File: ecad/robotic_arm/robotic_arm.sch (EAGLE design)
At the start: 121 parts, among them J1 5A/28V, SW1 5A/28V, Y1 16 MHz

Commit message: Update Robotic Arm to use new EAGLE library names.
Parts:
- A6: device PiB_radio_frequency:ANTENNA_SMD_CHP-2.45GHZ-0.5DBI-3W -> _radio_frequency:ANTENNA_SMD_CHP-2.45GHZ-0.5DBI-3W
- AVR_ISP: device PiB_connectors:AVR_SPI_PRG_6_PTH_VERT_MALE_2.54MM -> _connectors:AVR_SPI_PRG_6_PTH_VERT_MALE_2.54MM
- B1: device PiB_radio_frequency:BALUN_SMD-0805_UNBAL/BAL-50/100 -> _radio_frequency:BALUN_SMD-0805_UNBAL/BAL-50/100
- C1, C10, C12, C14, C16, C19, C2, C22, C24, C26, C28, C3, C30, C4, C47, C48, C49, C5, C50, C51, C52, C54, C6, C63, C7, C79, C83, C85, C93, C96, C98: device PiB_capacitors:0.1UF_SMD-0402_50V-10% -> _capacitors:0.1UF_SMD-0402_50V-10%
- C11, C13, C15, C17, C9: device PiB_capacitors:100UF-POLARIZED_SMD_25V-20%_DIA5-LS2-H11 -> _capacitors:100UF-POLARIZED_SMD_25V-20%_DIA5-LS2-H11
- C18, C25, C29, C8, C92: device PiB_capacitors:10UF_CER_SMD-0402_6.3V-20% -> _capacitors:10UF_CER_SMD-0402_6.3V-20%
- C20, C27, C80: device PiB_capacitors:1000UF-POLARIZED_PTH_16V-20% -> _capacitors:1000UF-POLARIZED_PTH_16V-20%
- C21, C23, C55, C57, C58: device PiB_capacitors:1UF_CER_SMD-0402_25V-10% -> _capacitors:1UF_CER_SMD-0402_25V-10%
- C53: value 1uF/25V -> 0.1uF/50V; device PiB_capacitors:1UF_CER_SMD-0402_25V-10% -> _capacitors:0.1UF_SMD-0402_50V-10%
- C59, C60: device PiB_capacitors:12PF_SMD-0402_100V-5% -> _capacitors:12PF_SMD-0402_100V-5%
- C61: device PiB_capacitors:22PF_CER_SMD-0402-100V-5% -> _capacitors:22PF_CER_SMD-0402-100V-5%
- C62: device PiB_capacitors:0.75PF_CER_SMD-0402_50V-33% -> _capacitors:0.75PF_CER_SMD-0402_50V-33%
- C94, C95, C97: device PiB_capacitors:10UF_CER_SMD-0805_25V-10% -> _capacitors:10UF_CER_SMD-0805_25V-10%
- D1: device PiB_discrete_semiconductors:DIODE_GENERAL-PURPOSE_SMD-0402_GP_150MA-75V -> _discrete_semiconductors:GENERAL-PURPOSE_SMD-0402_GP_150MA-75V
- D2, D7: device PiB_discrete_semiconductors:DIODE_GENERAL-PURPOSE_SMD_GP_1A-50V -> _discrete_semiconductors:GENERAL-PURPOSE_SMD_GP_1A-50V
- DEMUX1: device PiB:CD74HC4067-SM96_16:1_MUX-DEMUX_SOP-24_16:1-MUX-DEMUX -> _special:CD74HC4067-SM96_16:1_MUX-DEMUX_SOP-24_16:1-MUX-DEMUX
- FSR_INDEX, FSR_MIDDLE, FSR_PALM, FSR_PINKY, FSR_RING, FSR_THUMB: device PiB_sensors:FORCE-SENSITIVE-RESISTOR_SENSOR_FSR-5MM_0530470210_VERT-MALE_PITCH-1.25MM -> _sensors:FORCE-SENSITIVE-RESISTOR_SENSOR_FSR-5MM_0530470210_VERT-MALE_PITCH-1.25MM
- J1: device PiB_connectors:POWER_JACK-BARREL_ID2.1MM-OD5.5MM_PTH_ID2.1MM-OD5.5MM -> _connectors:POWER_JACK-BARREL_ID2.1MM-OD5.5MM_PTH_ID2.1MM-OD5.5MM
- JP1: device PiB_connectors:FTDI_PTH_VERT_MALE_2.54MM -> _connectors:FTDI_PTH_RA-MALE
- JP2: device PiB_connectors:JUMPER_SMD_2-PAD_NO_SILK -> _connectors:JUMPER_SMD_2-PAD_NO_SILK
- JP3: value JUMPER_SMD_3-PAD_NO_NO-SILK -> JUMPER_SMD_3-PAD_NO_SILK; device PiB_connectors:JUMPER_SMD_3-PAD_NO_NO-SILK -> _connectors:JUMPER_SMD_3-PAD_NO_SILK
- L1, L2: device PiB_inductors:10UH_SMD-0603_0.38A-0.468OHM-10% -> _inductors:10UH_SMD-0603_0.38A-0.468OHM-10%
- LED1: device PiB_leds:LED_SMD-0402_DISCRETE_BLUE -> _leds:LED_SMD-0402_DISCRETE_BLUE
- LIPO1: device PiB_batteries:BATTERY_LIPO_2S_2S_7.4V_PTH-PADS_AWG-18 -> _batteries:BATTERY_LIPO_2S_2S_7.4V_PTH-PADS_AWG-18
- MCU: device PiB_ic_microcontrollers:ATMEGA128RFA1_VFQFN-64_EXPOSED-PAD -> _ic_microcontrollers:ATMEGA128RFA1_VFQFN-64_EXPOSED-PAD
- NOISE_BR, NOISE_BR1: device PiB_power_symbols:NET_BRIDGE -> _power_symbols:NET_BRIDGE
- PWM_DRIVER: device PiB:PCA9685_16-CH_12-BIT_PWM-DRIVER_TSSOP-28_PWM-DRIVER_16CH -> _special:PCA9685_16-CH_12-BIT_PWM-DRIVER_TSSOP-28_PWM-DRIVER_16CH
- R1, R10, R12, R14, R16, R39, R4, R40, R41, R42, R43, R6, R8: device PiB_resistors:10KΩ_SMD-0402_1/16W-5% -> _resistors:10KΩ_SMD-0402_1/16W-5%
- R13, R15, R5, R7, R9: device PiB_resistors:100Ω_SMD-0402_1/16W-5% -> _resistors:100Ω_SMD-0402_1/16W-5%
- R17, R18: device PiB_resistors:4.7KΩ_SMD-0402_1/16W-5% -> _resistors:4.7KΩ_SMD-0402_1/16W-5%
- R2, R3: device PiB_resistors:1KΩ_SMD-0402_1/16W-5% -> _resistors:1KΩ_SMD-0402_1/16W-5%
- RX_LED: device PiB_leds:LED_SMD-0402_DISCRETE_RED -> _leds:LED_SMD-0402_DISCRETE_RED
- SERVO_INDEX, SERVO_MIDDLE, SERVO_PINKY, SERVO_RING, SERVO_THUMB: device PiB_motors:SERVO_HK15298B_PTH_VERT_MALE_2.54MM -> _motors:SERVO_HK15298B_PTH_VERT_MALE_2.54MM
- SW1: device PiB_switches:SWITCH_SPDT_VERT_PTH_5A-28V_13L-7W_ -> _switches:SWITCH_SPDT_VERT_PTH_5A-28V_13L-7W_
- TEMP_INDEX, TEMP_MIDDLE, TEMP_PINKY, TEMP_RING, TEMP_THUMB: device PiB_sensors:TEMPERATURE-SENSOR_TMP36_TMP36_PTH_VERT -> _sensors:TEMPERATURE-SENSOR_TMP36_TMP36_PTH_VERT
- TX_LED: device PiB_leds:LED_SMD-0402_DISCRETE_GREEN -> _leds:LED_SMD-0402_DISCRETE_GREEN
- VREG-ANALOG: device PiB_ic_power:VREG_LINEAR_MCP1700_MCP1700T-1802_1.8V-200MA_SOT-23 -> _ic_power:VREG_LINEAR_MCP1700_MCP1700T-1802_1.8V-200MA_SOT-23
- VREG-MCU: device PiB_ic_power:VREG_TPS768XX_ULDO_FAST-TRANSIENT_TPS76833QDR_1A-3.3V -> _ic_power:VREG_TPS768XX_ULDO_FAST-TRANSIENT_TPS76833QDR_1A-3.3V
- VREG-SERVOS: device PiB_ic_power:VREG_MIC29501-5.0_LINEAR_ULDO_5A-5V_MC29501-5.0_5A-5V -> _ic_power:VREG_MIC29501-5.0_LINEAR_ULDO_5A-5V_MC29501-5.0_5A-5V
- Y1: device PiB_crystals_oscillators_resonators:CRYSTAL_ABM3B_16MHZ_18PF -> _crystals_oscillators_resonators:CRYSTAL_ABM3B_16MHZ_18PF
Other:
- moved on the sheet: SERVO_INDEX, SERVO_MIDDLE, SERVO_PINKY, SERVO_RING, SERVO_THUMB, TEMP_INDEX, TEMP_MIDDLE, TEMP_PINKY, TEMP_RING, TEMP_THUMB

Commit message: Remove components that I believe are unecessary or redundant.
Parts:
- removed C18, C25: 10uF/6.3V, _capacitors:10UF_CER_SMD-0402_6.3V-20%
- removed R12, R14, R4, R6, R8: 10K, _resistors:10KΩ_SMD-0402_1/16W-5%
- removed R13, R15, R5, R7, R9: 100, _resistors:100Ω_SMD-0402_1/16W-5%
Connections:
- removed net N$4: R9.1, SERVO_THUMB.SIG
- removed net N$6: R7.1, SERVO_INDEX.SIG
- removed net N$7: R5.1, SERVO_MIDDLE.SIG
- removed net N$8: R15.1, SERVO_RING.SIG
- removed net N$9: R13.1, SERVO_PINKY.SIG
- net 3.3V: no longer C25.1
- net A3.3V: no longer C18.1
- net AGND: no longer C18.2
- net GND: no longer C25.2, R12.1, R14.1, R4.1, R6.1, R8.1
- net SERVO_INDEX: now also SERVO_INDEX.SIG; no longer R6.2, R7.2
- net SERVO_MIDDLE: now also SERVO_MIDDLE.SIG; no longer R4.2, R5.2
- net SERVO_PINKY: now also SERVO_PINKY.SIG; no longer R12.2, R13.2
- net SERVO_RING: now also SERVO_RING.SIG; no longer R14.2, R15.2
- net SERVO_THUMB: now also SERVO_THUMB.SIG; no longer R8.2, R9.2
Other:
- moved on the sheet: C1, C10, C11, C12, C13, C14, C15, C16, C17, C19, C27, C79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

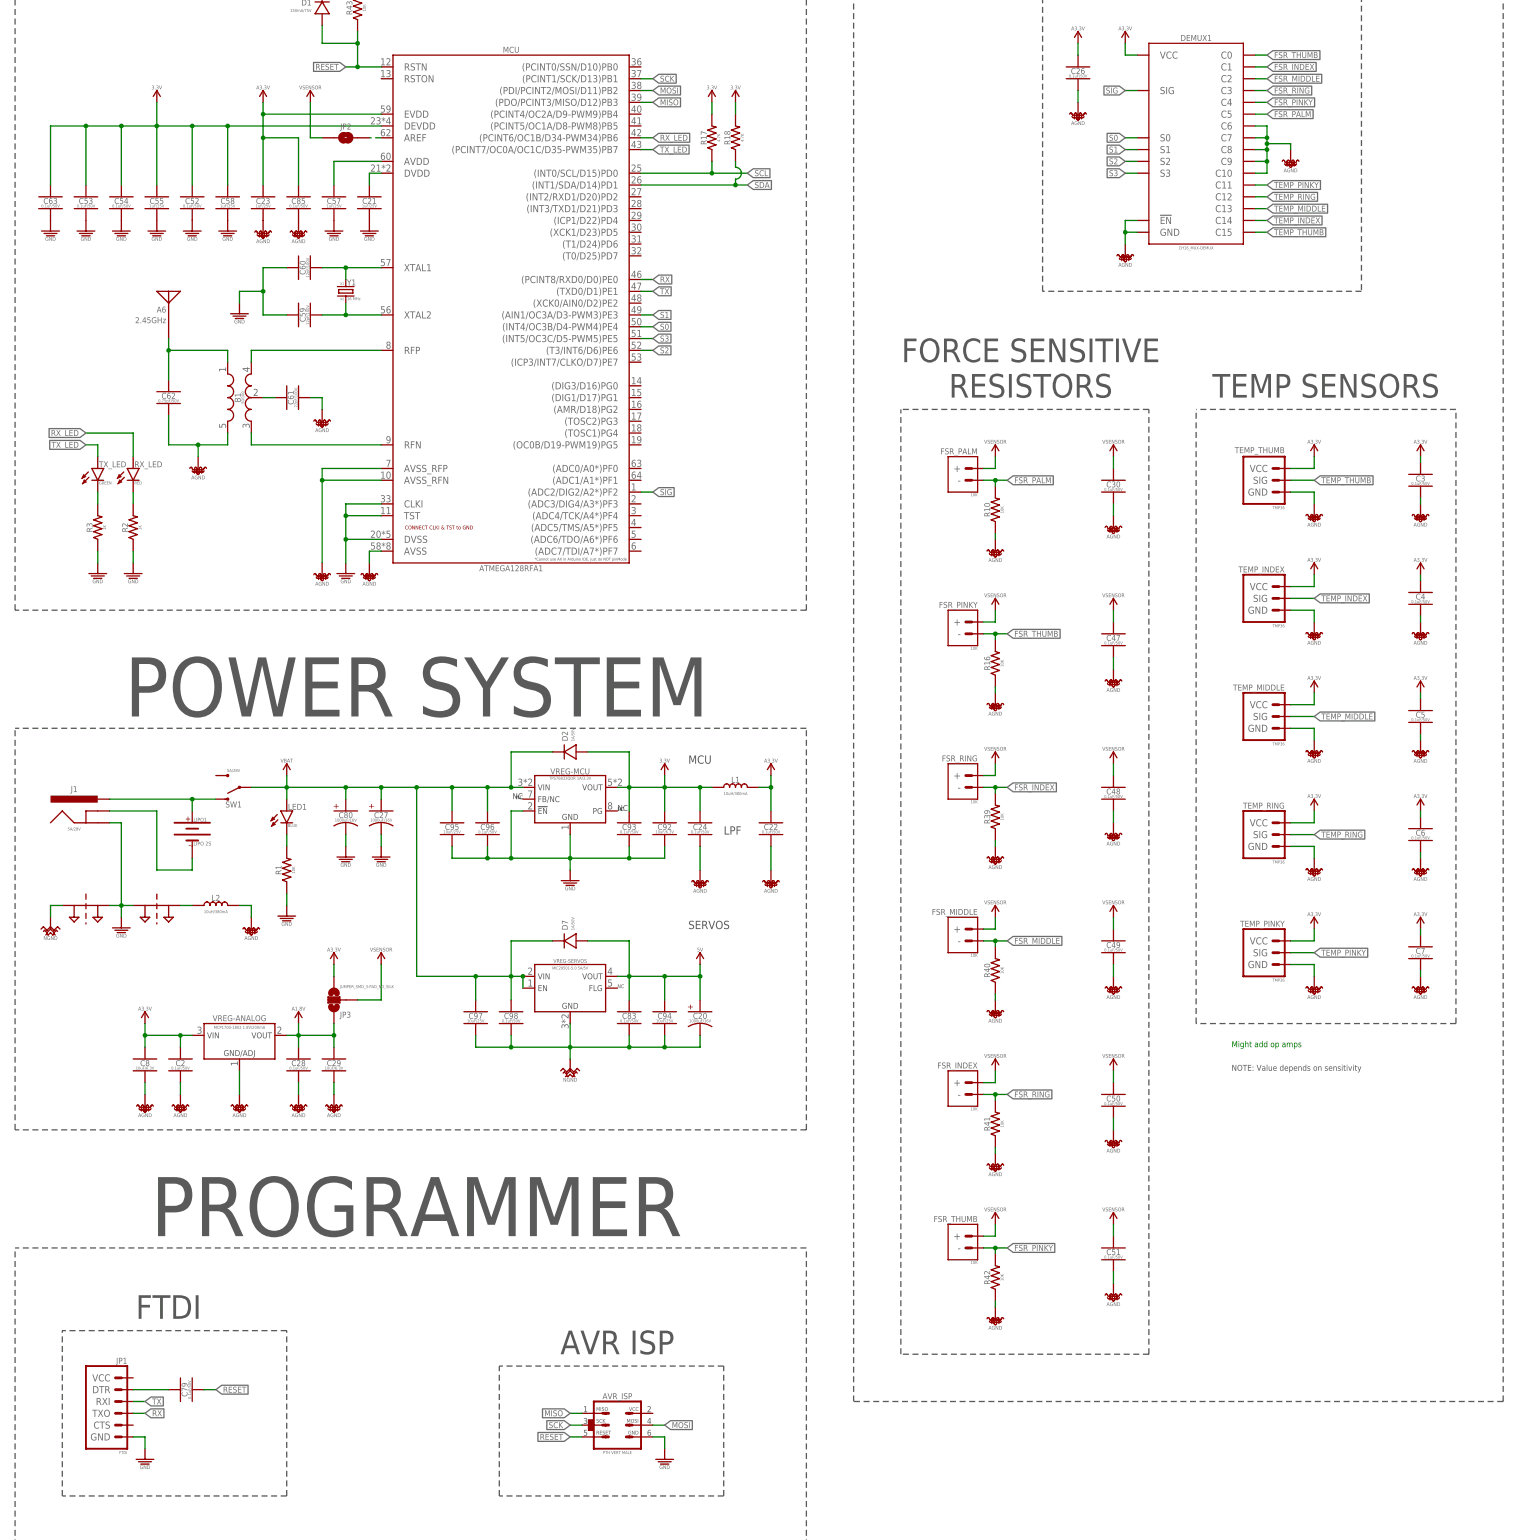
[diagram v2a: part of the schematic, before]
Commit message: Create mcu to unity example code.  Create schematics for master thesis.  Edit robotic arm and touch glove pcb.
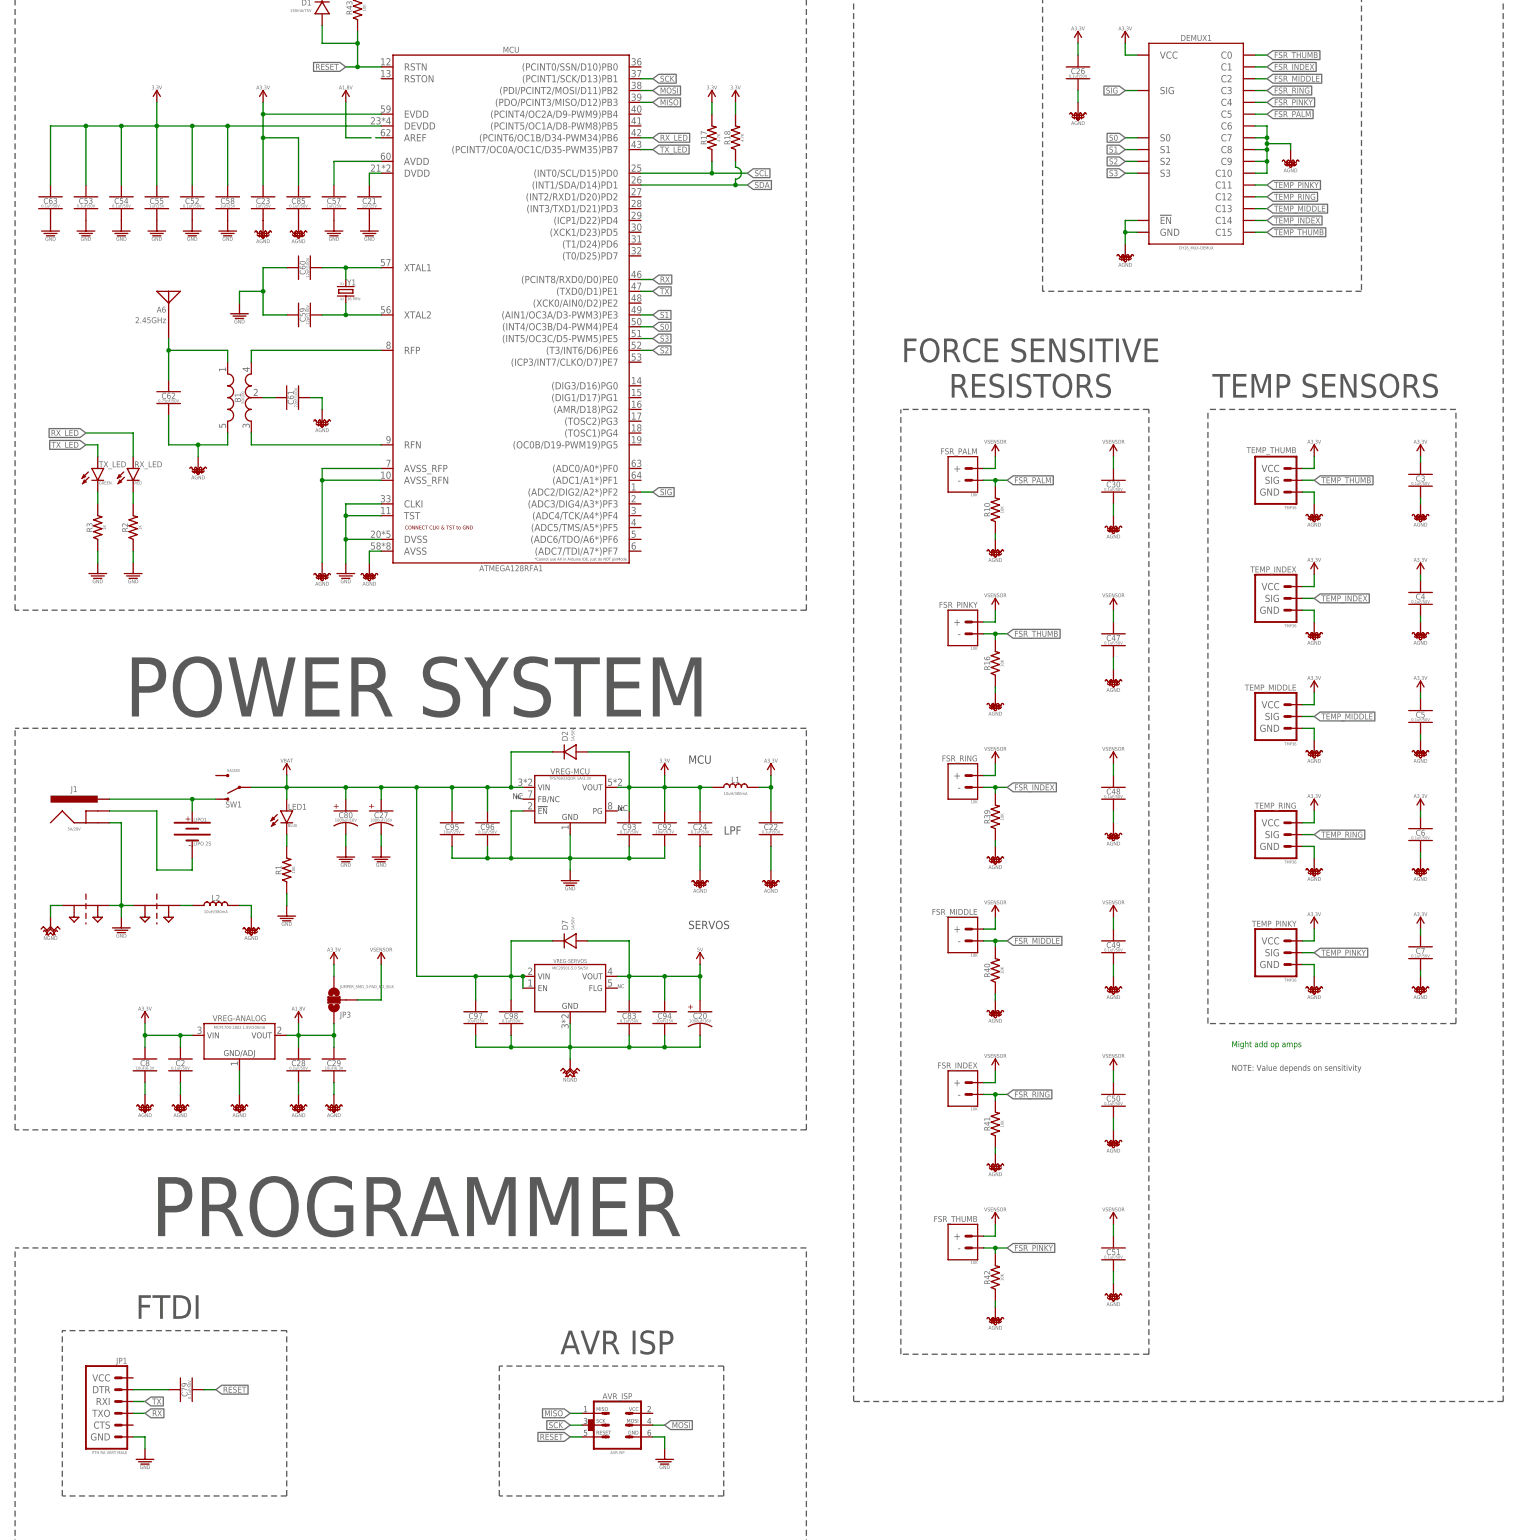
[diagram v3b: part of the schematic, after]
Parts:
- removed JP2: JUMPER_SMD_2-PAD_NO_SILK, _connectors:JUMPER_SMD_2-PAD_NO_SILK
- AVR_ISP: value PTH VERT MALE -> AVR ISP
- JP1: value FTDI -> PTH RA VERT MALE; device _connectors:FTDI_PTH_RA-MALE -> _connectors:FTDI_PTH_RA_MALE_2.54MM
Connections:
- removed net AREF: JP2.2, MCU.AREF
- net A1.8V: now also MCU.AREF
- net VSENSOR: no longer JP2.1
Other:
- moved on the sheet: TEMP_INDEX, TEMP_MIDDLE, TEMP_PINKY, TEMP_RING, TEMP_THUMB
